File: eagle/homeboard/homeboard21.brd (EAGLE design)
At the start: 93.5 x 71.8 mm, 133 parts, among them IC1 XCF02S, IC2 25LC080SN, IC3 ATMEGA32U2-TQFP, Q5 BC848SMD, Q6 BC848SMD, Q7 BC848SMD, Q8 BC848SMD, T1 BSS138, T2 BC848, T3 BSS138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

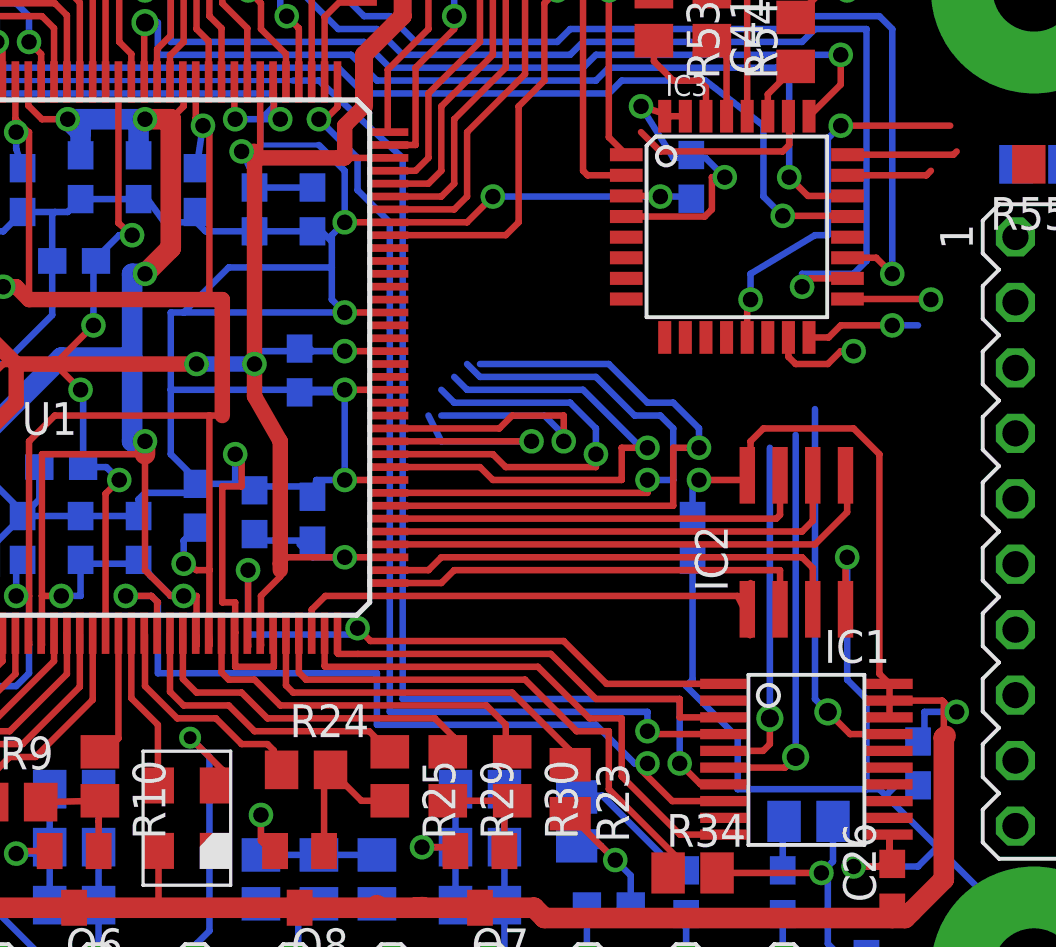
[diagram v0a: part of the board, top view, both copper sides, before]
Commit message: power to bottom right chips
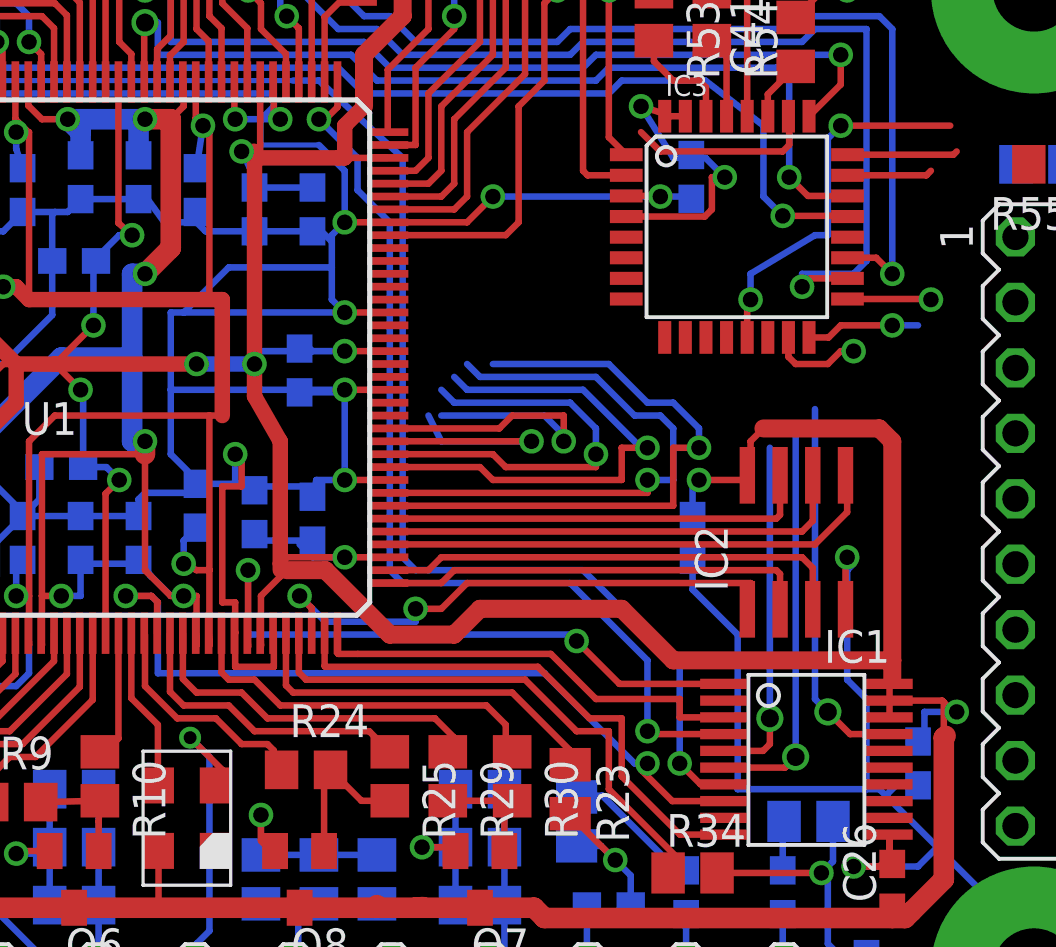
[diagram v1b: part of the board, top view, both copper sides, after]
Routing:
- net VCC: track 475.8 -> 502.7 mm
- net N$40: track 60.1 -> 57.6 mm
- net TDO_FPGA: track 39.8 -> 37.7 mm
- net PROM_INITB: track 32.3 -> 31.2 mm
- net FL_SEL: track 22.4 -> 21.5 mm, vias 0 -> 2
- net W6: track 24.6 -> 24.1 mm

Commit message: stuff
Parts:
- moved C29 1.50 mm to (77.2, 26.8)
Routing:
- net VCC: track 502.7 -> 510.0 mm, vias 23 -> 24
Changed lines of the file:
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@@
 <element name="C27" library="rcl" package="C0603" value="100nF" x="75.7019" y="40.7625625" rot="MR270"/>
 <element name="C28" library="rcl" package="C0603" value="100nF" x="97" y="35.5"/>
-<element name="C29" library="rcl" package="C0603" value="100nF" x="75.75" y="26.75" rot="MR270"/>
+<element name="C29" library="rcl" package="C0603" value="100nF" x="77.25" y="26.75" rot="MR270"/>
 <element name="C30" library="rcl" package="C0603" value="100nF" x="96.5" y="2.25" rot="R270"/>
 <element name="C31" library="rcl" package="C0603" value="100nF" x="98" y="38"/>
@@
 <via x="68" y="40" extent="1-16" drill="0.6" shape="square"/>
 <wire x1="68" y1="40" x2="74.5" y2="40" width="0.254" layer="16"/>
-<wire x1="88.28" y1="25.73" x2="81.98" y2="25.73" width="0" layer="19" extent="1-16"/>
 <wire x1="81.98" y1="25.73" x2="81.75" y2="25.5" width="0.254" layer="16"/>
-<wire x1="77.5" y1="17" x2="77.5" y2="23" width="0.254" layer="16"/>
-<wire x1="77.5" y1="23" x2="75.75" y2="24.75" width="0.254" layer="16"/>
-<wire x1="75.75" y1="25.9" x2="75.75" y2="24.75" width="0.254" layer="16"/>
+<wire x1="77.5" y1="17" x2="77.5" y2="25.5" width="0.254" layer="16"/>
+<wire x1="77.5" y1="25.5" x2="77.1" y2="25.9" width="0.254" layer="16"/>
+<wire x1="77.25" y1="25.9" x2="77.1" y2="25.9" width="0.254" layer="16"/>
+<wire x1="77.1" y1="25.9" x2="77" y2="26" width="0.254" layer="16"/>
 <wire x1="81" y1="65.5" x2="95.73" y2="78.43" width="0" layer="19" extent="16-16"/>
 <wire x1="17.5" y1="64.5" x2="17.5" y2="64.25" width="0" layer="19" extent="16-16"/>
@@
 <wire x1="57.225" y1="17.145" x2="57.5" y2="17.5" width="0" layer="19" extent="1-1"/>
 <wire x1="71.68" y1="9.08" x2="71.65" y2="6.65" width="0" layer="19" extent="16-16"/>
+<wire x1="88.28" y1="25.73" x2="81.98" y2="25.73" width="0" layer="19" extent="16-16"/>
 <wire x1="95" y1="22" x2="88.28" y2="25.73" width="0" layer="19" extent="1-1"/>
 <wire x1="98" y1="18.73" x2="95" y2="22" width="0" layer="19" extent="1-1"/>
@@
 <wire x1="84.25" y1="12.25" x2="85.5" y2="13.5" width="0.8" layer="1"/>
 <wire x1="85.5" y1="13.5" x2="85.5" y2="19" width="0.8" layer="1"/>
-<wire x1="75.75" y1="27.6" x2="75.75" y2="28.75" width="0.254" layer="16"/>
-<wire x1="75.75" y1="28.75" x2="76" y2="29" width="0.254" layer="16"/>
-<via x="76" y="29" extent="1-16" drill="0.6" shape="square"/>
-<wire x1="76" y1="29" x2="77.69474375" y2="29" width="0.254" layer="1"/>
+<via x="76.25" y="29" extent="1-16" drill="0.6" shape="square"/>
+<wire x1="76.25" y1="29" x2="77" y2="29" width="0.254" layer="1"/>
+<wire x1="77" y1="29" x2="77.69474375" y2="29" width="0.254" layer="1"/>
 <wire x1="77.69474375" y1="29" x2="77.875325" y2="29.18058125" width="0.254" layer="1"/>
 <wire x1="84.1" y1="12.4" x2="84.25" y2="12.25" width="0.254" layer="1"/>
@@
 <wire x1="60" y1="25.5" x2="61.5" y2="25.5" width="0.7" layer="1"/>
 <wire x1="61.5" y1="25.5" x2="64" y2="23" width="0.7" layer="1"/>
-<wire x1="64" y1="23" x2="66.5" y2="23" width="0.7" layer="1"/>
-<wire x1="66.5" y1="23" x2="67.5" y2="24" width="0.7" layer="1"/>
-<wire x1="67.5" y1="24" x2="73" y2="24" width="0.7" layer="1"/>
-<wire x1="73" y1="24" x2="75" y2="22" width="0.7" layer="1"/>
-<wire x1="75" y1="22" x2="83.5" y2="22" width="0.7" layer="1"/>
+<wire x1="64" y1="23" x2="74" y2="23" width="0.7" layer="1"/>
+<wire x1="74" y1="23" x2="75" y2="22" width="0.7" layer="1"/>
+<wire x1="75" y1="22" x2="76" y2="22" width="0.7" layer="1"/>
+<wire x1="76" y1="22" x2="83.5" y2="22" width="0.7" layer="1"/>
 <wire x1="83.5" y1="22" x2="83.5" y2="21.25" width="0.7" layer="1"/>
-<wire x1="78.5" y1="31" x2="83" y2="31" width="0.7" layer="1"/>
-<wire x1="83" y1="31" x2="83.5" y2="30.5" width="0.7" layer="1"/>
+<wire x1="77.5" y1="31" x2="83" y2="31" width="0.254" layer="1"/>
+<wire x1="83" y1="31" x2="83.5" y2="30.5" width="0.254" layer="1"/>
 <wire x1="83.5" y1="30.5" x2="83.5" y2="22" width="0.7" layer="1"/>
 <wire x1="83.393396875" y1="21.087409375" x2="83.393396875" y2="21.143396875" width="0.254" layer="1"/>
 <wire x1="83.393396875" y1="21.143396875" x2="83.5" y2="21.25" width="0.254" layer="1"/>
-<wire x1="78" y1="29.30525625" x2="78" y2="30.5" width="0.254" layer="1"/>
-<wire x1="78" y1="30.5" x2="78.5" y2="31" width="0.254" layer="1"/>
+<via x="76" y="24" extent="1-16" drill="0.6" shape="square"/>
+<wire x1="76" y1="24" x2="76" y2="22" width="0.254" layer="1"/>
+<wire x1="76" y1="24" x2="76" y2="28.5" width="0.254" layer="16"/>
+<wire x1="76" y1="28.5" x2="76" y2="29" width="0.254" layer="16"/>
+<wire x1="77.25" y1="27.6" x2="76.9" y2="27.6" width="0.254" layer="16"/>
+<wire x1="76.9" y1="27.6" x2="76" y2="28.5" width="0.254" layer="16"/>
+<wire x1="77.5" y1="31" x2="77" y2="30.5" width="0.254" layer="1"/>
+<wire x1="77" y1="30.5" x2="77" y2="29" width="0.254" layer="1"/>
 <wire x1="97.45" y1="42.5" x2="98.27" y2="78.43" width="0" layer="19" extent="1-1"/>
 <wire x1="97.15" y1="38" x2="97.45" y2="42.5" width="0" layer="19" extent="1-1"/>
@@
 <wire x1="88.28" y1="15.57" x2="85.5" y2="13.5" width="0" layer="19" extent="1-1"/>
 <wire x1="90.82" y1="15.57" x2="88.28" y2="15.57" width="0" layer="19" extent="1-1"/>
-<wire x1="76.223221875" y1="39.223221875" x2="78.5" y2="31" width="0" layer="19" extent="1-1"/>
+<wire x1="76.223221875" y1="39.223221875" x2="77.5" y2="31" width="0" layer="19" extent="1-1"/>
 <wire x1="96.5" y1="3.1" x2="90.82" y2="15.57" width="0" layer="19" extent="1-1"/>
 </signal>
@@
 <contactref element="U1" pad="P72"/>
 <contactref element="IC1" pad="3"/>
-<wire x1="70.25" y1="22.25" x2="62.77" y2="22.25" width="0.254" layer="1"/>
 <wire x1="76.943396875" y1="19.787409375" x2="75.25" y2="19.787409375" width="0.254" layer="1"/>
 <wire x1="75.25" y1="19.787409375" x2="75.25" y2="20.5" width="0.254" layer="1"/>
 <wire x1="75.25" y1="20.5" x2="72" y2="20.5" width="0.254" layer="1"/>
 <wire x1="72" y1="20.5" x2="70.25" y2="22.25" width="0.254" layer="1"/>
-<wire x1="61.97" y1="23.05" x2="61.97" y2="22.28" width="0.254" layer="1"/>
-<wire x1="61.97" y1="22.28" x2="62" y2="22.25" width="0.254" layer="1"/>
-<wire x1="62" y1="22.25" x2="62.75" y2="22.25" width="0.254" layer="1"/>
-<wire x1="62.75" y1="22.25" x2="62.77" y2="22.25" width="0" layer="19" extent="1-1"/>
+<wire x1="70.25" y1="22.25" x2="62" y2="22.25" width="0.254" layer="1"/>
+<wire x1="62" y1="22.25" x2="62" y2="23" width="0.254" layer="1"/>
+<wire x1="61.97" y1="23.05" x2="61.97" y2="23.03" width="0.254" layer="1"/>
+<wire x1="61.97" y1="23.03" x2="62" y2="23" width="0.254" layer="1"/>
 </signal>
 <signal name="N$38">
@@
 <wire x1="58.5" y1="22.52" x2="58.47" y2="23.05" width="0.254" layer="1"/>
 <wire x1="58.5" y1="22.52" x2="58.5" y2="25.5" width="0.254" layer="1"/>
-<via x="71.25" y="22.75" extent="1-16" drill="0.6" shape="square"/>
-<wire x1="71.25" y1="22.75" x2="71" y2="23" width="0.254" layer="16"/>
+<via x="72.5" y="21.5" extent="1-16" drill="0.6" shape="square"/>
+<wire x1="72.5" y1="21.5" x2="71" y2="23" width="0.254" layer="16"/>
 <wire x1="76.943396875" y1="21.087409375" x2="72.912590625" y2="21.087409375" width="0.254" layer="1"/>
-<wire x1="72.912590625" y1="21.087409375" x2="71.25" y2="22.75" width="0.254" layer="1"/>
+<wire x1="72.912590625" y1="21.087409375" x2="72.5" y2="21.5" width="0.254" layer="1"/>
 </signal>
 <signal name="VCCINT">

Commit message: mah
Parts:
- moved U$8 2.00 mm to (89.0, 50.0)
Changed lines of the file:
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@@
 <element name="U$1" library="cpcfpga" package="GNDHOLE" value="GNDHOLE" x="12.5" y="17"/>
 <element name="U$7" library="cpcfpga" package="GNDHOLE" value="GNDHOLE" x="4.5" y="54.5"/>
-<element name="U$8" library="cpcfpga" package="GNDHOLE" value="GNDHOLE" x="89" y="48"/>
+<element name="U$8" library="cpcfpga" package="GNDHOLE" value="GNDHOLE" x="89" y="50"/>
 <element name="U$9" library="cpcfpga" package="GNDHOLE" value="GNDHOLE" x="89" y="10"/>
 <element name="SV5" library="con-lstb" package="MA05-2" value="" x="36.25" y="13.25" rot="R270">
@@
 <wire x1="80.2" y1="50" x2="80.2" y2="54.3" width="0.254" layer="16"/>
 <wire x1="80.2" y1="54.3" x2="79.5" y2="55" width="0.254" layer="16"/>
-<wire x1="89" y1="48" x2="82.2" y2="48" width="0.254" layer="16"/>
+<wire x1="89" y1="50" x2="82.2" y2="48" width="0.254" layer="16"/>
 <wire x1="82.2" y1="48" x2="80.2" y2="50" width="0.254" layer="16"/>
 <wire x1="82.2" y1="48" x2="81.75" y2="48" width="0.254" layer="16"/>
